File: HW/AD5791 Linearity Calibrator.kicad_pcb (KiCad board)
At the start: 4 copper layers, 85 x 68 mm, 57 parts, among them J1 OUTPUT, J10 Conn_01x01, J2 PWR, J3 REF, J4 REF, J5 REF, J6 REF, J7 Conn_01x01, J8 Conn_01x01, J9 Conn_01x01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

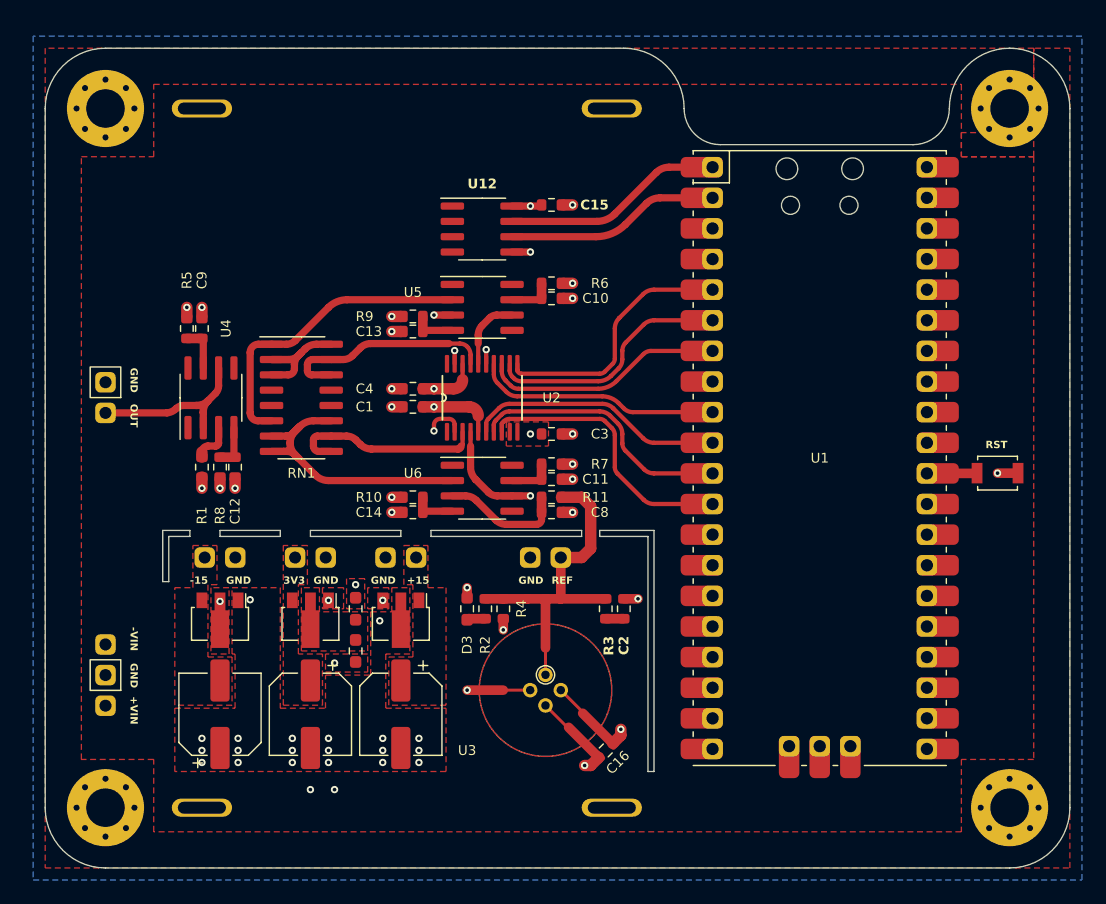
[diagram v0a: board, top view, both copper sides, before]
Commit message: 4 wire buffer, keepout under isolator traces
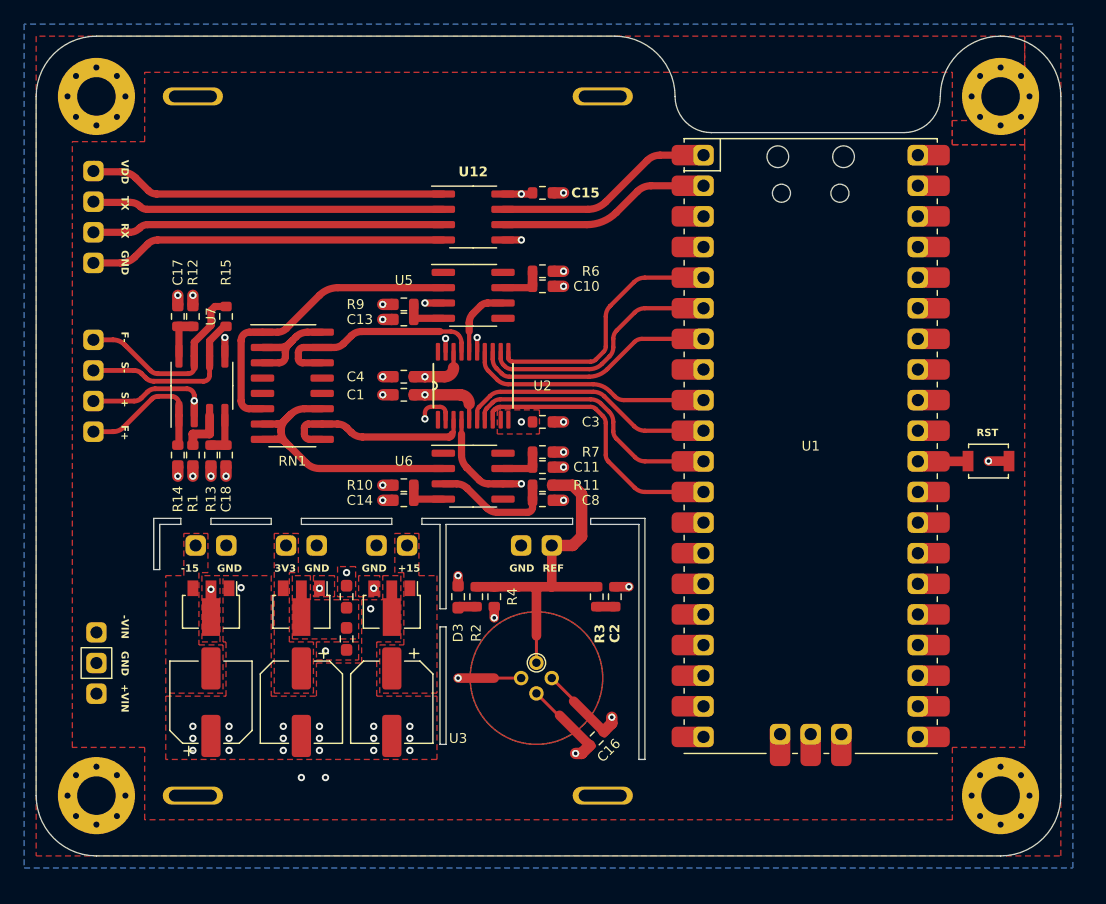
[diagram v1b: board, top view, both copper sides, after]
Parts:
- removed C12, C9: 10uF, Resistor_SMD:R_0603_1608Metric
- removed J1: OUTPUT, Connector_PinHeader_2.54mm:PinHeader_1x02_P2.54mm_Vertical
- removed R5, R8: 10R, Resistor_SMD:R_0603_1608Metric
- removed U4: OPA189, Package_SO:SOIC-8_3.9x4.9mm_P1.27mm
- added C17: 10uF, Resistor_SMD:R_0603_1608Metric, F.Cu at (123.0, 94.2)
- added C18: 10uF, Resistor_SMD:R_0603_1608Metric, F.Cu at (127.0, 105.8)
- added J11: ISO OUT, Connector_PinHeader_2.54mm:PinHeader_1x04_P2.54mm_Vertical, F.Cu at (116.0, 82.2)
- added J12: ISO OUT, Connector_PinHeader_2.54mm:PinHeader_1x04_P2.54mm_Vertical, F.Cu at (116.0, 103.8)
- added R12: 10R, Resistor_SMD:R_0603_1608Metric, F.Cu at (124.2, 94.2)
- added R13: 10R, Resistor_SMD:R_0603_1608Metric, F.Cu at (125.8, 105.8)
- added R14: 100K, Resistor_SMD:R_0603_1608Metric, F.Cu at (123.0, 105.8)
- added R15: 100K, Resistor_SMD:R_0603_1608Metric, F.Cu at (127.0, 94.2)
- added U7: OPA2140, Package_SO:SOIC-8_3.9x4.9mm_P1.27mm, F.Cu at (125.0, 100.0)
- moved C1 1.25 mm to (141.8, 100.8)
- moved C10 1.25 mm to (153.2, 91.8)
- moved C11 1.25 mm to (153.2, 106.8)
- moved C13 1.25 mm to (141.8, 94.5)
- moved C14 1.25 mm to (141.8, 109.5)
- moved C15 1.25 mm to (153.2, 84.0)
- moved C16 1.25 mm to (157.8, 129.2)
- moved C2 1.25 mm to (159.2, 117.5)
- moved C3 1.25 mm to (153.2, 103.0)
- moved C4 1.25 mm to (141.8, 99.2)
- moved C5 1.25 mm to (140.8, 126.2)
- moved C6 1.25 mm to (125.8, 126.2)
- moved C7 1.25 mm to (133.2, 126.2)
- moved C8 1.25 mm to (153.2, 109.5)
- moved D1 1.25 mm to (137.0, 121.0)
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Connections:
- U12 pad 1: unconnected-(U12-VDD1-Pad1) -> /ISO_VDD
- U12 pad 2: unconnected-(U12-VOA-Pad2) -> /ISO_TX
- U12 pad 3: unconnected-(U12-VIB-Pad3) -> /ISO_RX
- U12 pad 4: unconnected-(U12-GND1-Pad4) -> /ISO_GND
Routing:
- net /ISO_VDD: track 0.00 -> 30.3 mm
- net /ISO_GND: track 0.00 -> 29.7 mm
- net /ISO_RX: track 0.00 -> 29.2 mm
- net /ISO_TX: track 0.00 -> 29.2 mm
- net /SENSE+: track 0.00 -> 18.1 mm, vias 0 -> 2
- net /FORCE-: track 0.00 -> 16.4 mm
- net Net-(J1-Pin_1): track 15.9 -> 0.00 mm
- net /SENSE-: track 0.00 -> 14.9 mm
- net /FORCE+: track 0.00 -> 12.0 mm
- net Net-(U4A-V+): track 3.75 -> 0.00 mm
- net Net-(U7C-V+): track 0.00 -> 3.74 mm
- net Net-(U4A-V-): track 3.74 -> 0.00 mm
- net Net-(U7C-V-): track 0.00 -> 3.74 mm
- net GND: track 21.8 -> 23.4 mm, vias 39 -> 40
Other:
- outline, holes or cut-outs redrawn
- board text added: "F+"
- board text added: "F-"
- board text added: "RX"
- board text added: "S+"
- board text added: "S-"
- board text added: "TX"
- board text added: "VDD"
- board text removed: "OUT"

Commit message: Layout Rev 3
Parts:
- added C9: 10uF, Resistor_SMD:R_0603_1608Metric, F.Cu at (142.8, 86.0)
- moved J11 27.9 mm to (143.7, 79.0), turned to 90 degrees
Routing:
- net /ISO_VDD: track 30.3 -> 0.62 mm
- net /ISO_TX: track 29.2 -> 8.12 mm
- net /ISO_RX: track 29.2 -> 10.1 mm
- net /ISO_GND: track 29.7 -> 13.4 mm
- added copper zone on F.Cu, net /ISO_GND
- added copper zone on F.Cu, net /ISO_VDD

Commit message: added blank notes space
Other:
- board text added: "AD5791 LINEARITY CALIBRATOR NNNI 3132"
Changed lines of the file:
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@@
     (effects (font (size 0.6096 0.6096) (thickness 0.1016) bold) (justify left bottom))
+  )
+  (gr_text "AD5791 LINEARITY CALIBRATOR\nNNNI 3132" (at 194.75 126.75 90) (layer "F.Mask")
+    (effects (font (size 0.8128 0.8128) (thickness 0.1524) bold) (justify left))
   )
   (segment (start 154.25 105.5) (end 155 105.5) (width 0.95) (layer "F.Cu") (net 1))

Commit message: blank space v2
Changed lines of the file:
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@@
     )
   )
+  (gr_line (start 138 88) (end 124 88)
+    (stroke (width 0.5) (type default)) (layer "F.Cu"))
+  (gr_line (start 140 81) (end 140 86)
+    (stroke (width 0.5) (type default)) (layer "F.Cu"))
+  (gr_arc (start 124 88) (mid 122.585786 87.414214) (end 122 86)
+    (stroke (width 0.5) (type default)) (layer "F.Cu"))
+  (gr_arc (start 138 79) (mid 139.414214 79.585786) (end 140 81)
+    (stroke (width 0.5) (type default)) (layer "F.Cu"))
+  (gr_line (start 124 79) (end 138 79)
+    (stroke (width 0.5) (type default)) (layer "F.Cu"))
+  (gr_line (start 122 86) (end 122 81)
+    (stroke (width 0.5) (type default)) (layer "F.Cu"))
+  (gr_arc (start 140 86) (mid 139.414214 87.414214) (end 138 88)
+    (stroke (width 0.5) (type default)) (layer "F.Cu"))
+  (gr_arc (start 122 81) (mid 122.585786 79.585786) (end 124 79)
+    (stroke (width 0.5) (type default)) (layer "F.Cu"))
   (gr_line (start 161.25 111.5) (end 161.25 131)
     (stroke (width 0.1) (type default)) (layer "Edge.Cuts"))
@@
       )
     )
+  )
+  (zone (net 0) (net_name "") (layer "F.Mask") (hatch edge 0.5)
+    (priority 9)
+    (connect_pads yes (clearance 0.127))
+    (min_thickness 0.127) (filled_areas_thickness no)
+    (fill yes (thermal_gap 0.127) (thermal_bridge_width 0.508) (smoothing fillet) (radius 2) (island_removal_mode 1) (island_area_min 9.999996))
+    (polygon
+      (pts
+        (xy 121.75 78.75)
+        (xy 121.75 88.25)
+        (xy 140.25 88.25)
+        (xy 140.25 78.75)
+      )
+    )

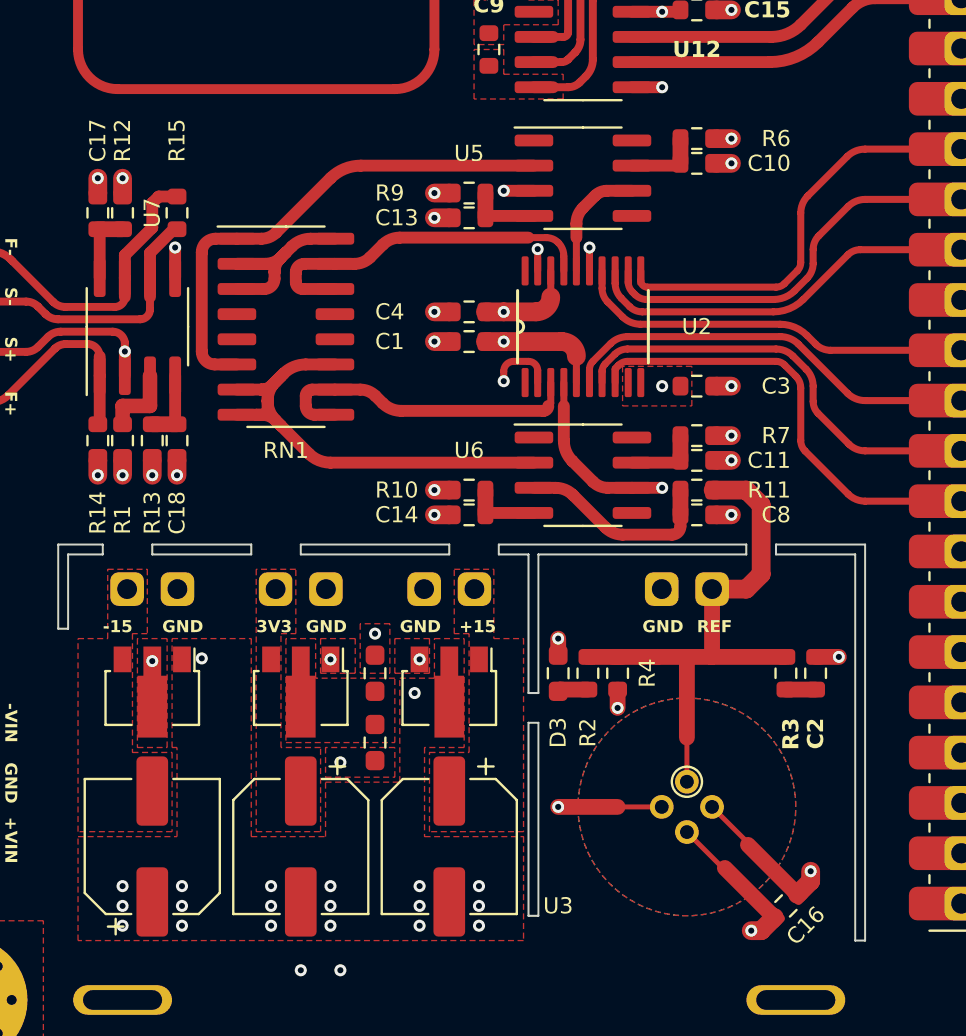
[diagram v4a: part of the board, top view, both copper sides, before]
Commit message: star ground added
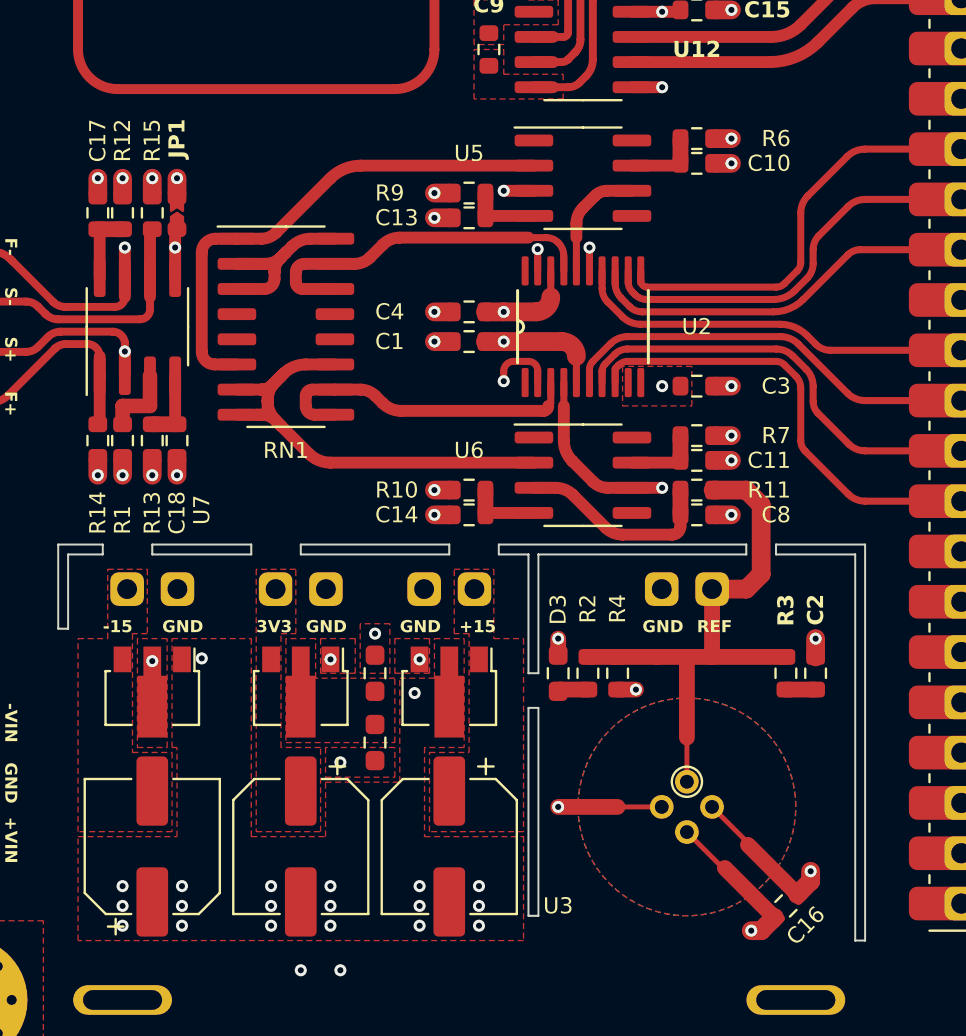
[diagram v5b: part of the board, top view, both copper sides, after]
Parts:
- added JP1: GND BRIDGE, 0603 Jumper:0603 Jumper, F.Cu at (127.0, 94.2)
- moved R15 1.25 mm to (125.8, 94.2)
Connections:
- C2 pad 2: GND -> GNDA
- C8 pad 2: GND -> GNDA
- U2 pad 19: GND -> GNDA
- U3 pad 2: GND -> GNDA
- U5 pad 3: GND -> GNDA
- U7 pad 5: GND -> GNDA
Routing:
- net GNDA: track 0.00 -> 151.7 mm, vias 0 -> 6
- net GND: track 23.4 -> 12.7 mm, vias 40 -> 35
- net /SENSE-: track 14.9 -> 14.3 mm
- net /FORCE-: track 16.4 -> 17.0 mm, vias 0 -> 2
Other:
- outline, holes or cut-outs redrawn

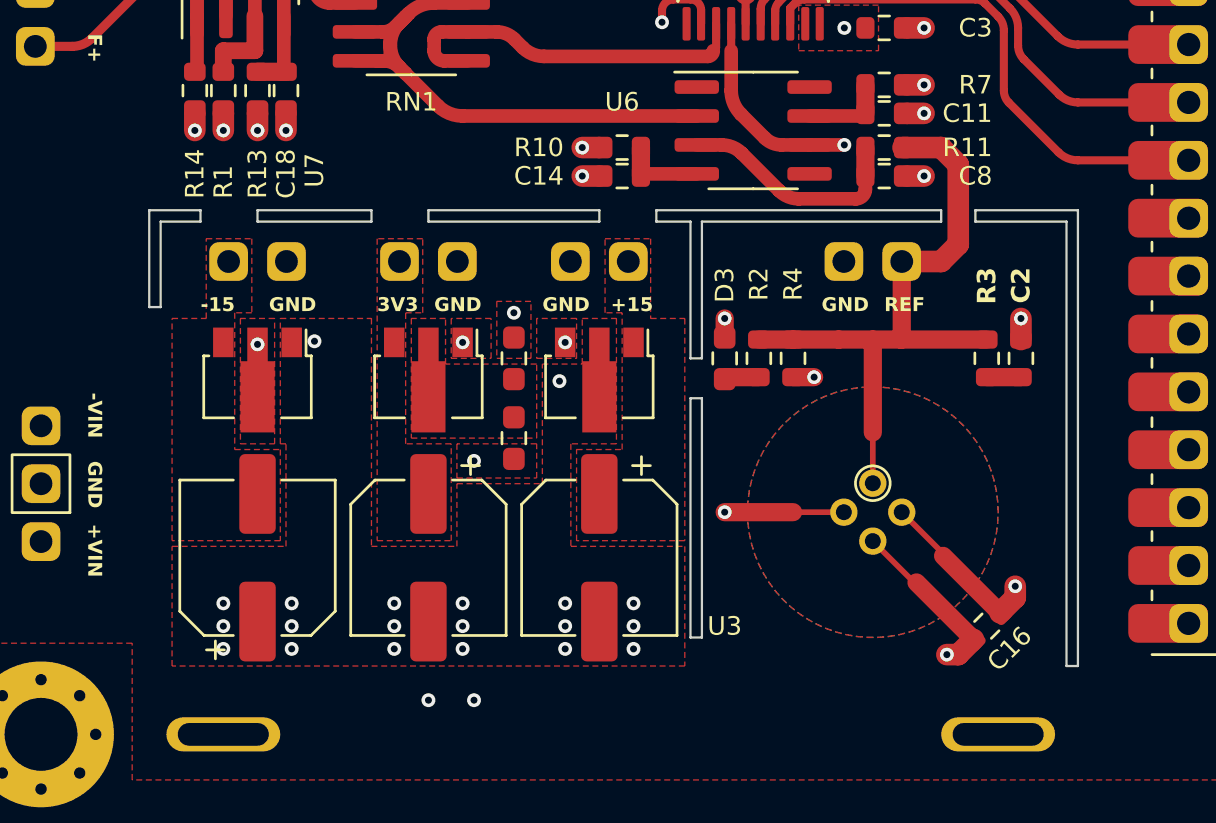
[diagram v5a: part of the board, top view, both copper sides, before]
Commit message: Widened slots for Aisler
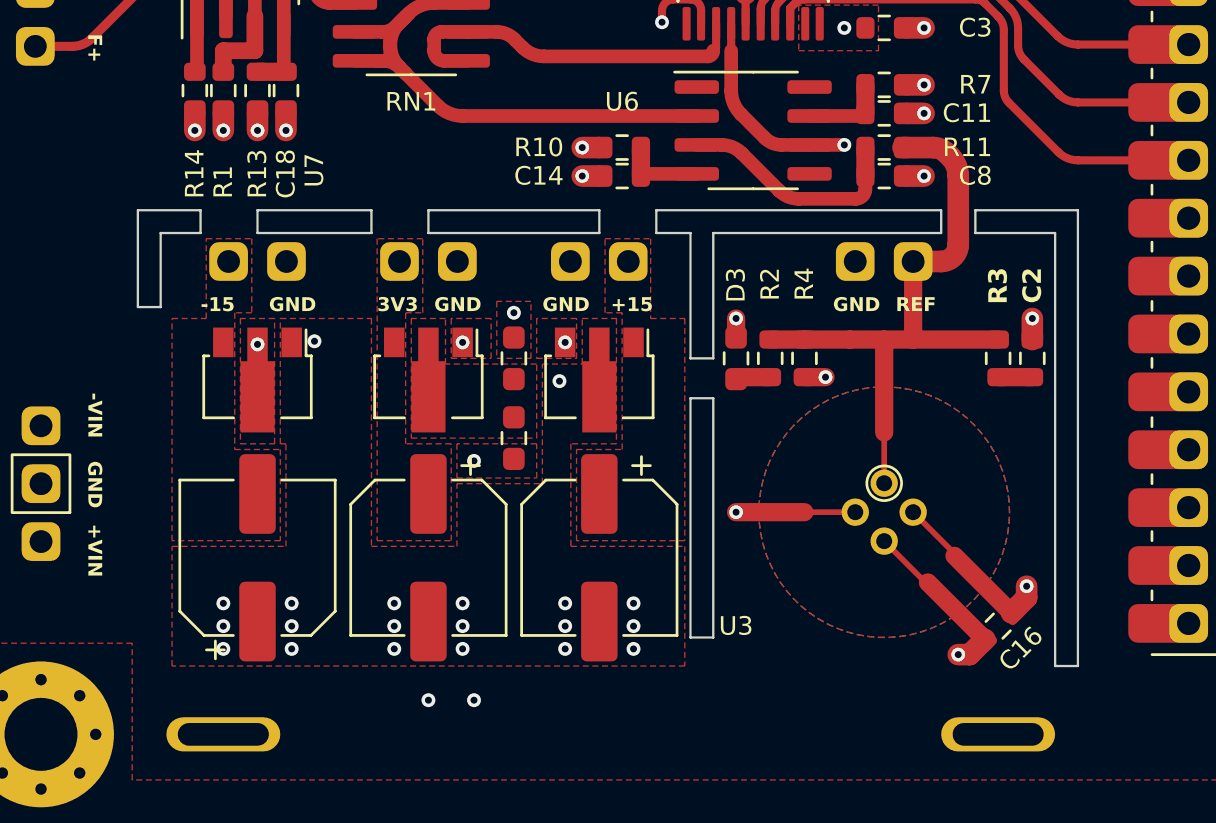
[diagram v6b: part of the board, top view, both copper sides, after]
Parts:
- moved C16 0.50 mm to (158.2, 129.2)
- moved C2 0.50 mm to (159.8, 117.5)
- moved D3 0.50 mm to (146.8, 117.5)
- moved J4 0.50 mm to (154.5, 113.2)
- moved R2 0.50 mm to (148.2, 117.5)
- moved R3 0.50 mm to (158.2, 117.5)
- moved R4 0.50 mm to (149.8, 117.5)
- moved U3 0.50 mm to (153.2, 123.0)
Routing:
- net /REF: track 28.8 -> 28.2 mm
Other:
- outline, holes or cut-outs redrawn

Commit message: Layout Rev 4
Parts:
- added D4: 5819, Resistor_SMD:R_0603_1608Metric_Pad0.98x0.95mm_HandSolder, F.Cu at (153.3, 104.2)
- R11: footprint Resistor_SMD:R_0603_1608Metric -> 0603 Jumper:0603 Jumper
- turned R11 to 0 degrees
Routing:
- net +15V: track 17.2 -> 23.8 mm
- net +3.3V: track 2.51 -> 5.35 mm
- net /VREFPF: track 31.6 -> 31.1 mm

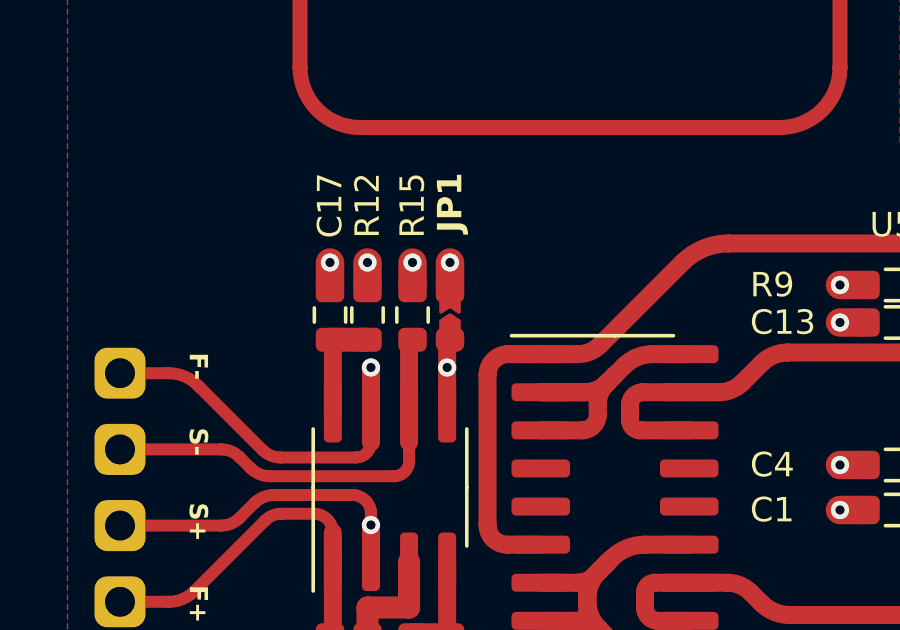
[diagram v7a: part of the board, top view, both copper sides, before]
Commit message: post-assembly touch ups
- ground coupling jumper now shorted by default
- software files updated with pinout
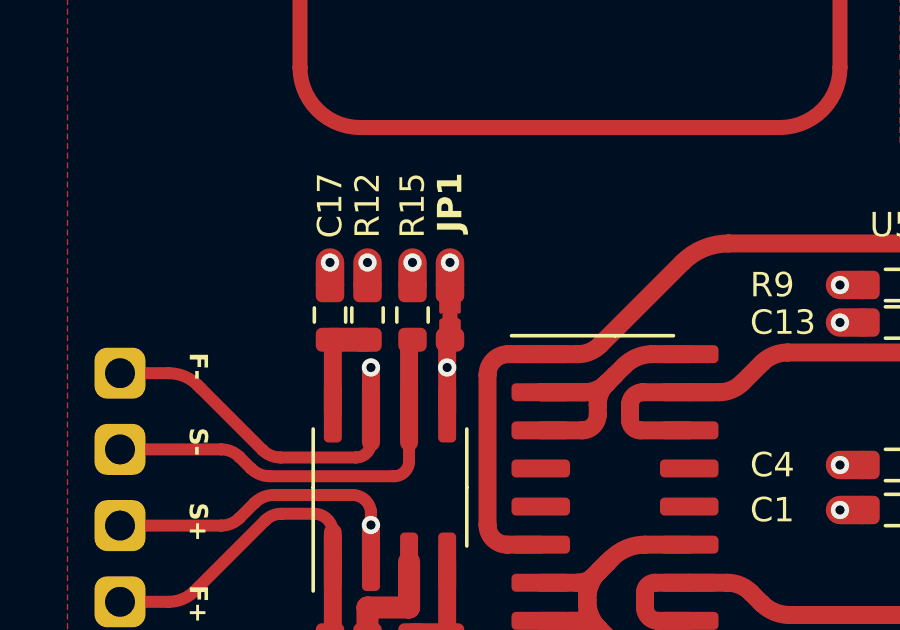
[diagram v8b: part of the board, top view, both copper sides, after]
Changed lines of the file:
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@@
   (gr_line (start 124 79) (end 138 79)
+    (stroke (width 0.5) (type default)) (layer "F.Cu"))
+  (gr_line (start 127 93.5) (end 127 95)
     (stroke (width 0.5) (type default)) (layer "F.Cu"))
   (gr_line (start 122 86) (end 122 81)
@@
     (pts (xy 111.25 65) (xy 196.25 65))
     (height 1.25)
-    (gr_text "3346.4567 mils" (at 153.75 64.45) (layer "Dwgs.User")
+    (gr_text "85.0000 mm" (at 153.75 64.45) (layer "Dwgs.User")
       (effects (font (size 1.5 1.5) (thickness 0.3)))
     )
@@
     (pts (xy 108.75 71) (xy 108.75 139.25))
     (height 1.25)
-    (gr_text "2687.0079 mils" (at 105.7 105.125 90) (layer "Dwgs.User")
+    (gr_text "68.2500 mm" (at 105.7 105.125 90) (layer "Dwgs.User")
       (effects (font (size 1.5 1.5) (thickness 0.3)))
     )
